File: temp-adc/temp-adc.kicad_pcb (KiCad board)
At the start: 2 copper layers, 22.9 x 33 mm, 23 parts, among them J1 Conn_01x06, U1 MCP3204

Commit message: SPI PCB final commit
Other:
- board text added: "April 2026, iaditya@stanford.edu"
- board text removed: "Josephine Zhao, Aditya Iyer April 2026, iaditya@stanford.edu"
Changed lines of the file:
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@@
 		)
 	)
-	(gr_text "Josephine Zhao, Aditya Iyer\nApril 2026, iaditya@stanford.edu"
+	(gr_text "April 2026, iaditya@stanford.edu"
 		(at 149.86 115.57 90)
 		(layer "B.SilkS")

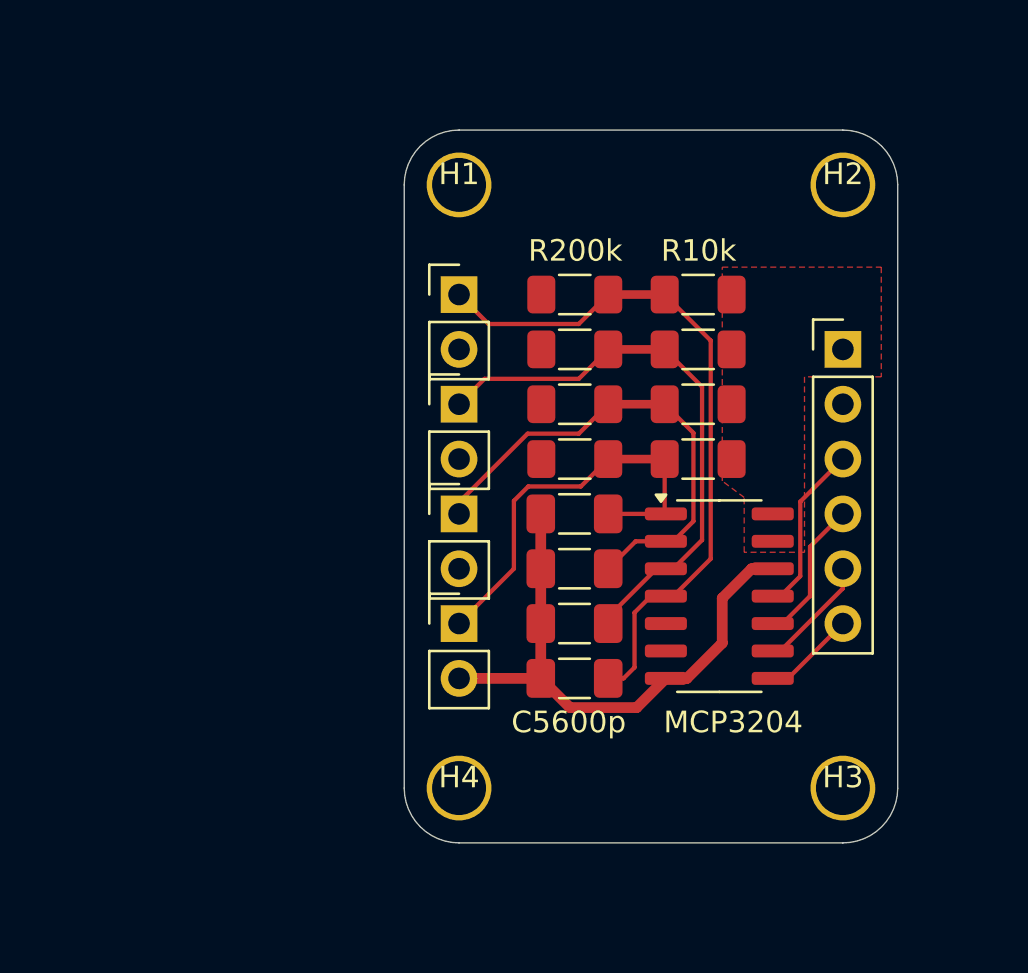
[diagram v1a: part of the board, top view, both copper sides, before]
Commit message: New PCB using MCP3428-SL
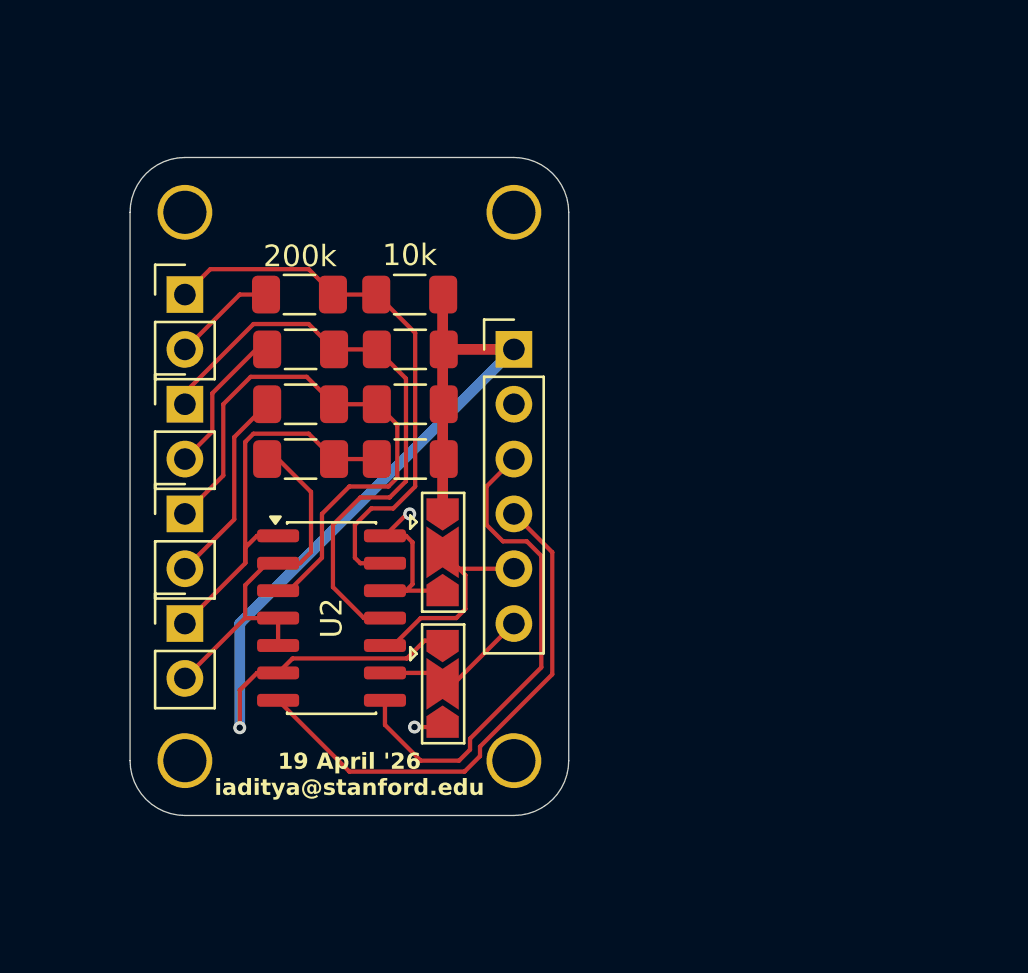
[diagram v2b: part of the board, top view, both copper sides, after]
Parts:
- removed C1, C2, C3, C4: 5600p, Capacitor_SMD:C_1206_3216Metric_Pad1.33x1.80mm_HandSolder
- removed U1: MCP3204, Package_SO:SOIC-14_3.9x8.7mm_P1.27mm
- added JP1: SolderJumper_3_Open, Jumper:SolderJumper-3_P2.0mm_Open_TrianglePad1.0x1.5mm, F.Cu at (138.9, 119.6)
- added JP2: SolderJumper_3_Open, Jumper:SolderJumper-3_P2.0mm_Open_TrianglePad1.0x1.5mm, F.Cu at (138.9, 113.5)
- added U2: MCP3428x-xSL, Package_SO:SOIC-14_3.9x8.7mm_P1.27mm, F.Cu at (133.8, 116.6)
- H1, H2, H3, H4: footprint MountingHole:MountingHole_M2.5_thinoutline -> footprints:MountingHole_M2_dia0.1in
- moved H3 30.5 mm to (127.0, 123.2)
- moved TH1 19.8 mm to (127.0, 101.6)
- moved TH4 19.8 mm to (127.0, 116.8)
- moved R1 15.4 mm to (137.4, 101.6)
- moved R7 15.4 mm to (137.4, 109.2)
- moved H2 15.3 mm to (142.2, 97.8)
- moved J1 15.2 mm to (142.2, 104.1)
- moved R2 14.9 mm to (132.3, 101.6)
- moved R8 14.8 mm to (132.4, 109.2)
- moved G*** 14.0 mm to (134.6, 101.6)
- moved TH2 13.7 mm to (127.0, 106.7)
- moved TH3 13.7 mm to (127.0, 111.8)
- moved R3 13.6 mm to (137.4, 104.1)
- moved R5 13.6 mm to (137.4, 106.7)
- moved R4 13.0 mm to (132.4, 104.1)
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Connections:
- J1 pad 3: /SCK -> /SCL
- J1 pad 4: /MISO -> /SDA
- J1 pad 5: /MOSI -> /A1
- J1 pad 6: /~{CS} -> /A0
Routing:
- net VCC: track 0.00 -> 48.1 mm, vias 0 -> 1
- net /SDA: track 0.00 -> 24.4 mm
- net /SCL: track 0.00 -> 23.0 mm
- net GND: track 26.6 -> 48.8 mm, vias 0 -> 2
- net /IN3: track 32.3 -> 18.8 mm
- net /A1: track 0.00 -> 11.1 mm
- net /SCK: track 7.90 -> 0.00 mm
- net /A0: track 0.00 -> 7.34 mm
- net /MISO: track 6.69 -> 0.00 mm
- net /IN0: track 19.8 -> 26.0 mm
- net /MOSI: track 5.36 -> 0.00 mm
- net /IN1: track 22.8 -> 28.0 mm
- net /~{CS}: track 4.30 -> 0.00 mm
- removed copper zone on F.Cu, net VCC
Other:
- board size 22.9 x 33 mm -> 20.3 x 30.5 mm
- board text added: "1+"
- board text added: "1-"
- board text added: "19 April '26 iaditya@stanford.edu"
- board text added: "4+"
- board text added: "4-"
- board text added: "A0"
- board text added: "A1"
- board text added: "SCL"
- board text added: "SDA"
- board text added: "Stanford SSI Polar Rover 4-channel Thermal DAQ v2 Zhao, Soerianto, Iyer"
- board text added: "Vcc"
- board text removed: "+1"
- board text removed: "+2"
- board text removed: "+3"
- board text removed: "+4"
- board text removed: "-1"
- board text removed: "-2"
- board text removed: "-3"
- board text removed: "-4"
- board text removed: "April 2026, iaditya@stanford.edu"
- board text removed: "C5600p"
- board text removed: "DI"
- board text removed: "DO"
- board text removed: "R10k"
- board text removed: "R200k"
- board text removed: "SCK"
- board text removed: "Stanford SSI Polar Rover 4-channel Thermal DAQ v1"
- board text removed: "Vin"
- board text removed: "~{CS}"
